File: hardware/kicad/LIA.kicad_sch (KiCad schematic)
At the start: 78 parts, among them J2 POGO-4P-FEM, Q1 8205A, Q2 AO3400A, Q3 AO3400A, Q4 AO3400A, U1 ESP32-S3-MINI-1-N8, U10 DW01A, U11 RT9080-33GJ5, U2 SAM-M10Q-00B, U3 Wio-SX1262, U5 TPD2EUSB30, U6 TYPE-C_16PIN_2MD(073), U7 RT9080-33GJ5, U8 TP4056, U9 MAX17048G+T10

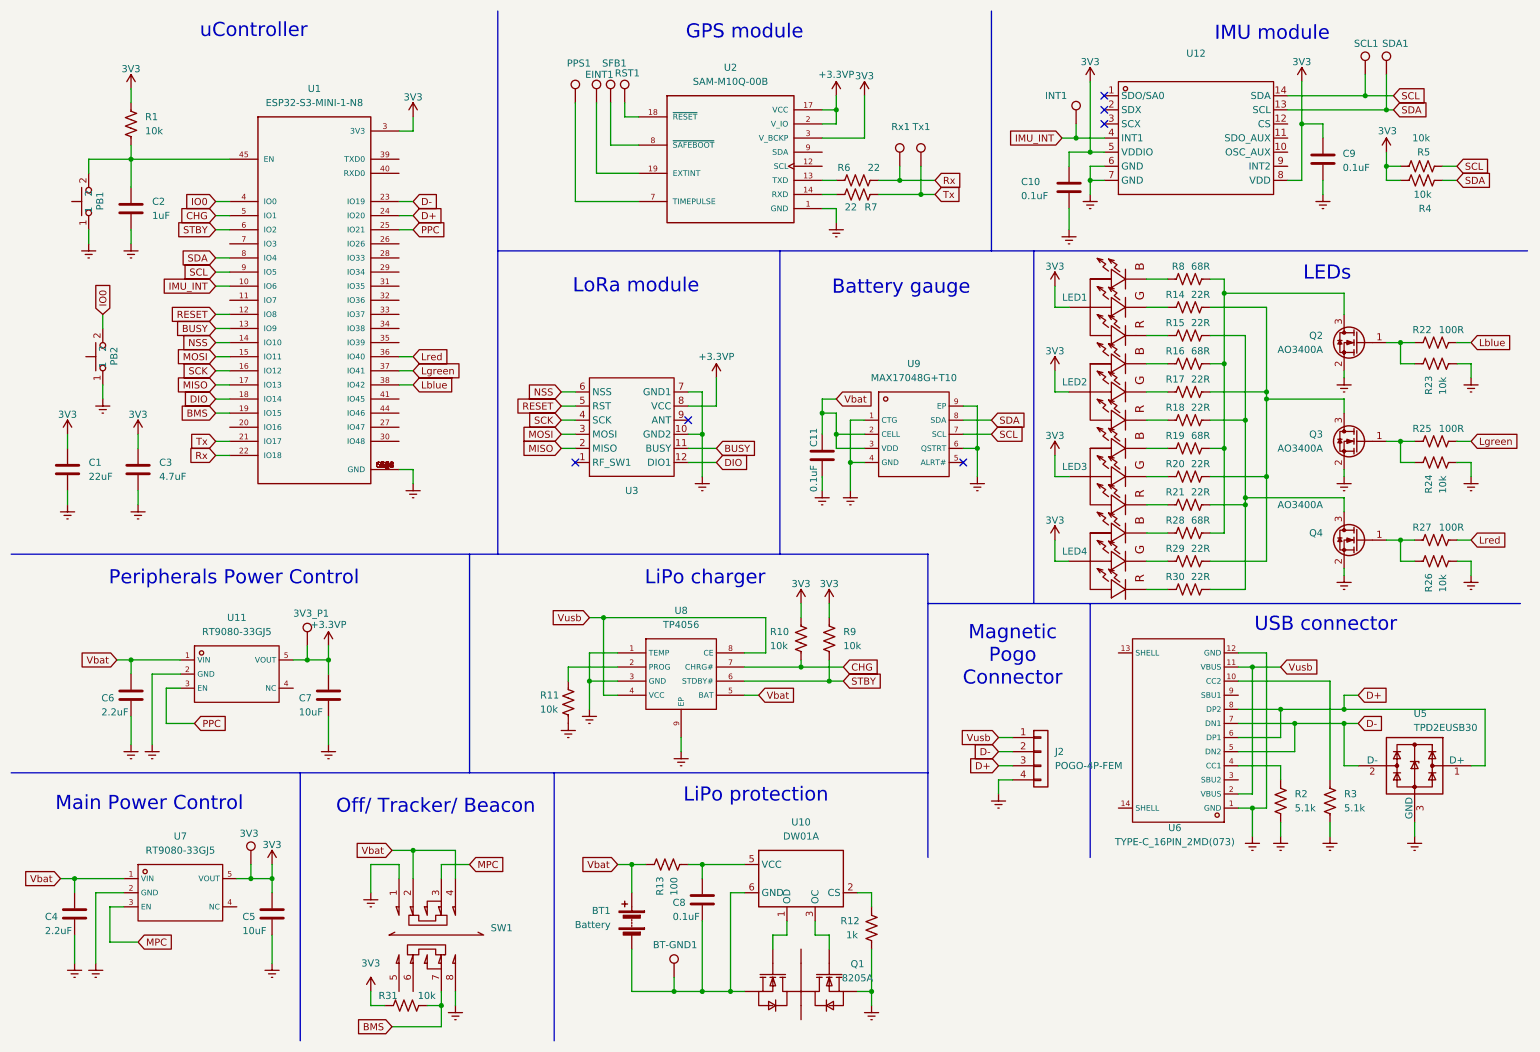
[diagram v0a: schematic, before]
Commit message: SDA/SCL corrected on IMU
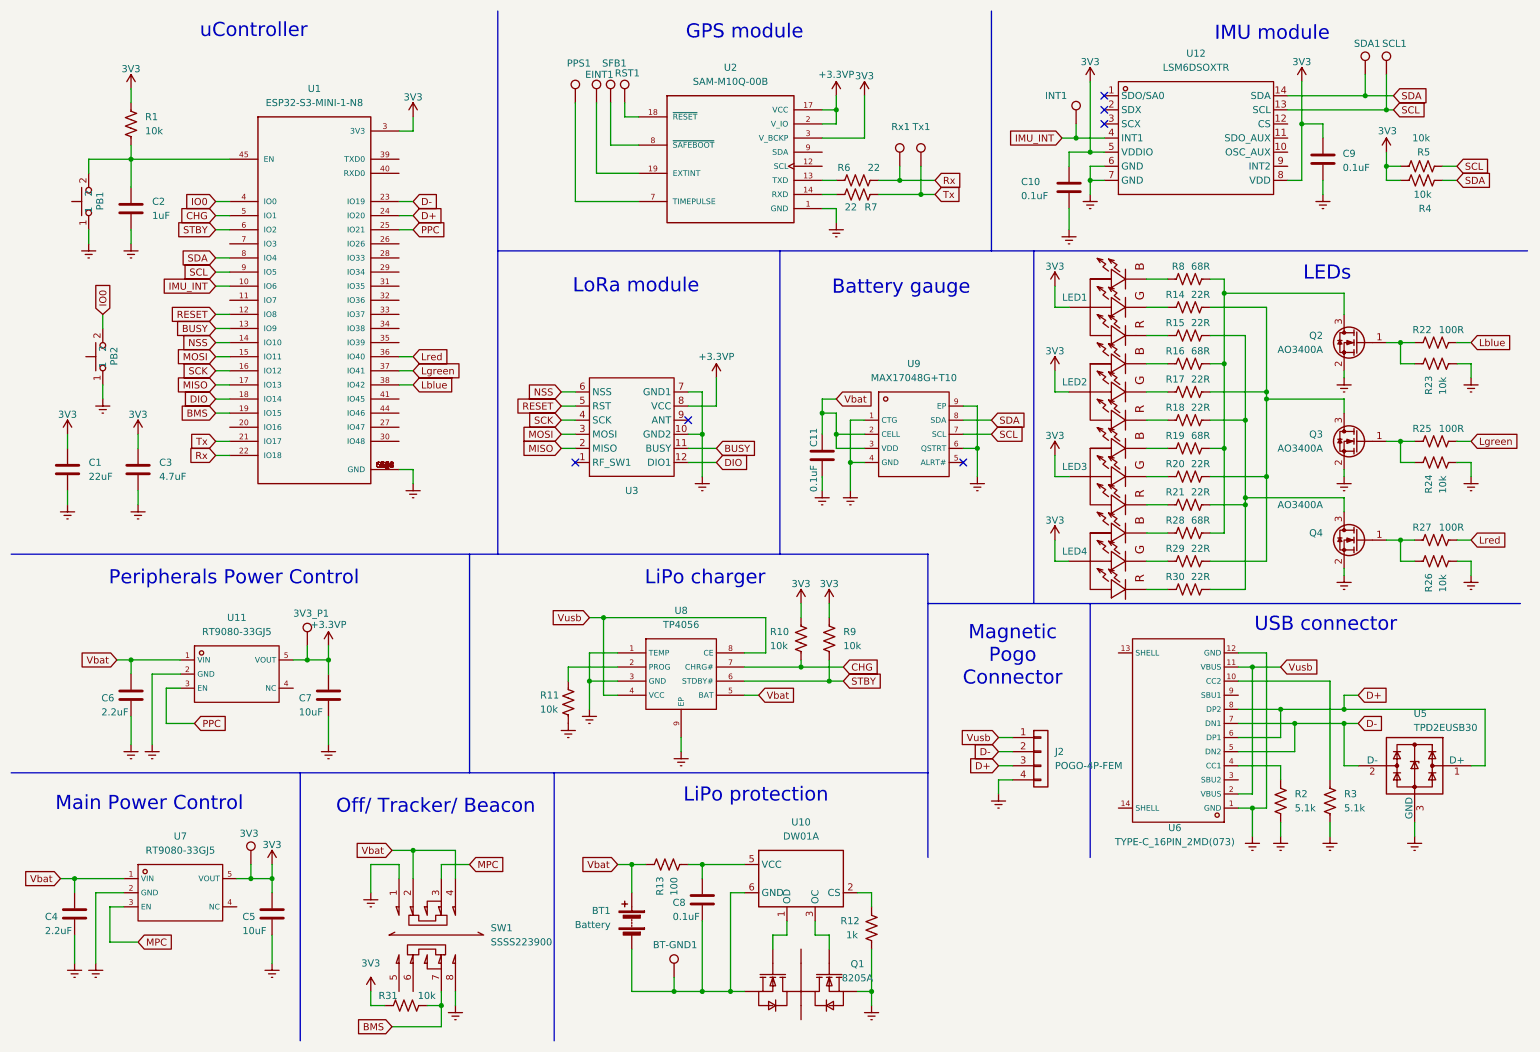
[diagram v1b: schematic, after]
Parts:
- LED1, LED2, LED3, LED4: value ~ -> MHS110CRGBCT
- SW1: value ~ -> SSSS223900
- U12: value ~ -> LSM6DSOXTR
- renumbered SDA1 to SCL1, SCL1 to SDA1
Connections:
- net SCL: now also SCL1.1, U12.13 (SCL); no longer SDA1.1, U12.14 (SDA)
- net SDA: now also SDA1.1, U12.14 (SDA); no longer SCL1.1, U12.13 (SCL)
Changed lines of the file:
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@@
 		)
 	)
-	(global_label "SDA"
+	(global_label "SCL"
 		(shape input)
 		(at 261.62 30.48 0)
@@
 		)
 	)
-	(global_label "SCL"
+	(global_label "SDA"
 		(shape input)
 		(at 261.62 27.94 0)
@@
 			)
 		)
-		(property "Value" "~"
+		(property "Value" "MHS110CRGBCT"
 			(at 212.1217 100.33 90)
 			(effects
@@
 			)
 		)
-		(property "Value" "~"
+		(property "Value" "LSM6DSOXTR"
 			(at 226.06 22.86 0)
 			(effects
@@
 			)
 		)
-		(property "Value" "~"
+		(property "Value" "MHS110CRGBCT"
 			(at 212.1217 85.09 90)
 			(effects
@@
 		(on_board yes)
 		(dnp no)
-		(property "Reference" "SCL1"
+		(property "Reference" "SDA1"
 			(at 254.508 18.542 0)
 			(effects
@@
 			(project "LIA"
 				(path "/2f540d84-795c-4606-8035-69185f828e9c"
-					(reference "SCL1")
+					(reference "SDA1")
 					(unit 1)
 				)
@@
 		(on_board yes)
 		(dnp no)
-		(property "Reference" "SDA1"
+		(property "Reference" "SCL1"
 			(at 259.588 18.542 0)
 			(effects
@@
 			(project "LIA"
 				(path "/2f540d84-795c-4606-8035-69185f828e9c"
-					(reference "SDA1")
+					(reference "SCL1")
 					(unit 1)
 				)
@@
 			)
 		)
-		(property "Value" "~"
+		(property "Value" "MHS110CRGBCT"
 			(at 212.1217 69.85 90)
 			(effects
@@
 			)
 		)
-		(property "Value" "~"
+		(property "Value" "MHS110CRGBCT"
 			(at 212.1217 54.61 90)
 			(effects
@@
 			)
 		)
-		(property "Value" "~"
+		(property "Value" "SSSS223900"
 			(at 99.06 180.3399 0)
 			(effects
